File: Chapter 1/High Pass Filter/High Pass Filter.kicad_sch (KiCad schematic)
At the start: 3 parts

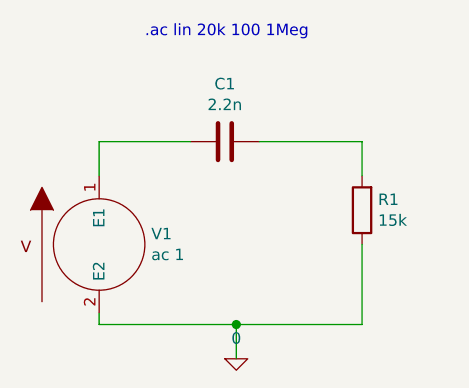
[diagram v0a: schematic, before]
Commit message: added v out tags to Chapter 1
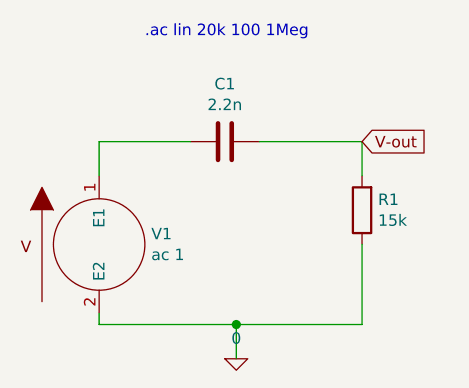
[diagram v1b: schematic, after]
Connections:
- net V-out: now reaches C1.1, R1.2
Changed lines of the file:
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@@
-(kicad_sch (version 20210406) (generator eeschema)
+(kicad_sch (version 20211123) (generator eeschema)
   (paper "A4")
-  (junction (at 95.25 63.5) (diameter 1.016) (color 0 0 0 0))
-  (wire (pts (xy 80.01 43.18) (xy 90.17 43.18))
+  (junction (at 95.25 63.5) (diameter 1.016) (color 0 0 0 0)
+  )
+  (wire (pts (xy 80.01 63.5) (xy 80.01 62.23))
+    (stroke (width 0) (type solid) (color 0 0 0 0))
+  )
+  (wire (pts (xy 109.22 63.5) (xy 95.25 63.5))
+    (stroke (width 0) (type solid) (color 0 0 0 0))
+  )
+  (wire (pts (xy 109.22 54.61) (xy 109.22 63.5))
     (stroke (width 0) (type solid) (color 0 0 0 0))
   )
@@
     (stroke (width 0) (type solid) (color 0 0 0 0))
   )
-  (wire (pts (xy 80.01 63.5) (xy 80.01 62.23))
+  (wire (pts (xy 95.25 63.5) (xy 80.01 63.5))
     (stroke (width 0) (type solid) (color 0 0 0 0))
   )
-  (wire (pts (xy 95.25 63.5) (xy 80.01 63.5))
+  (wire (pts (xy 80.01 43.18) (xy 90.17 43.18))
+    (stroke (width 0) (type solid) (color 0 0 0 0))
+  )
+  (wire (pts (xy 109.22 43.18) (xy 109.22 46.99))
+    (stroke (width 0) (type solid) (color 0 0 0 0))
+  )
+  (wire (pts (xy 97.79 43.18) (xy 109.22 43.18))
     (stroke (width 0) (type solid) (color 0 0 0 0))
   )
@@
     (stroke (width 0) (type solid) (color 0 0 0 0))
   )
-  (wire (pts (xy 97.79 43.18) (xy 109.22 43.18))
-    (stroke (width 0) (type solid) (color 0 0 0 0))
-  )
-  (wire (pts (xy 109.22 43.18) (xy 109.22 46.99))
-    (stroke (width 0) (type solid) (color 0 0 0 0))
-  )
-  (wire (pts (xy 109.22 54.61) (xy 109.22 63.5))
-    (stroke (width 0) (type solid) (color 0 0 0 0))
-  )
-  (wire (pts (xy 109.22 63.5) (xy 95.25 63.5))
-    (stroke (width 0) (type solid) (color 0 0 0 0))
-  )
   (text ".ac lin 20k 100 1Meg" (at 85.09 31.75 0)
     (effects (font (size 1.27 1.27)) (justify left bottom))
   )
-  (symbol (lib_id "High-Pass-Filter-rescue:0-pspice") (at 95.25 67.31 0) (unit 1)
+  (global_label "V-out" (shape input) (at 109.22 43.18 0) (fields_autoplaced)
+    (effects (font (size 1.27 1.27)) (justify left))
+    (property "Intersheet References" "${INTERSHEET_REFS}" (id 0) (at 117.5084 43.1006 0)
+      (effects (font (size 1.27 1.27)) (justify left) hide)
+    )
+  )
+  (symbol (lib_id "High-Pass-Filter-rescue:VSOURCE-pspice") (at 80.01 54.61 0) (unit 1)
     (in_bom yes) (on_board yes)
-    (property "Reference" "#GND01" (id 0) (at 95.25 69.85 0)
+    (property "Reference" "V1" (id 0) (at 85.8012 53.4416 0)
+      (effects (font (size 1.27 1.27)) (justify left))
+    )
+    (property "Value" "ac 1" (id 1) (at 85.8012 55.753 0)
+      (effects (font (size 1.27 1.27)) (justify left))
+    )
+    (property "Footprint" "" (id 2) (at 80.01 54.61 0)
       (effects (font (size 1.27 1.27)) hide)
     )
-    (property "Value" "0" (id 1) (at 95.25 65.0494 0))
-    (property "Footprint" "" (id 2) (at 95.25 67.31 0)
-      (effects (font (size 1.27 1.27)) hide)
-    )
-    (property "Datasheet" "~" (id 3) (at 95.25 67.31 0)
+    (property "Datasheet" "~" (id 3) (at 80.01 54.61 0)
       (effects (font (size 1.27 1.27)) hide)
     )
     (pin "1")
+    (pin "2")
+  )
+  (symbol (lib_id "High-Pass-Filter-rescue:C-Device") (at 93.98 43.18 270) (unit 1)
+    (in_bom yes) (on_board yes)
+    (property "Reference" "C1" (id 0) (at 93.98 36.7792 90))
+    (property "Value" "2.2n" (id 1) (at 93.98 39.0906 90))
+    (property "Footprint" "" (id 2) (at 90.17 44.1452 0)
+      (effects (font (size 1.27 1.27)) hide)
+    )
+    (property "Datasheet" "~" (id 3) (at 93.98 43.18 0)
+      (effects (font (size 1.27 1.27)) hide)
+    )
+    (pin "1")
+    (pin "2")
   )
   (symbol (lib_id "High-Pass-Filter-rescue:R-Device") (at 109.22 50.8 180) (unit 1)
@@
     (pin "2")
   )
-  (symbol (lib_id "High-Pass-Filter-rescue:C-Device") (at 93.98 43.18 270) (unit 1)
+  (symbol (lib_id "High-Pass-Filter-rescue:0-pspice") (at 95.25 67.31 0) (unit 1)
     (in_bom yes) (on_board yes)
-    (property "Reference" "C1" (id 0) (at 93.98 36.7792 90))
-    (property "Value" "2.2n" (id 1) (at 93.98 39.0906 90))
-    (property "Footprint" "" (id 2) (at 90.17 44.1452 0)
+    (property "Reference" "#GND01" (id 0) (at 95.25 69.85 0)
       (effects (font (size 1.27 1.27)) hide)
     )
-    (property "Datasheet" "~" (id 3) (at 93.98 43.18 0)
+    (property "Value" "0" (id 1) (at 95.25 65.0494 0))
+    (property "Footprint" "" (id 2) (at 95.25 67.31 0)
+      (effects (font (size 1.27 1.27)) hide)
+    )
+    (property "Datasheet" "~" (id 3) (at 95.25 67.31 0)
       (effects (font (size 1.27 1.27)) hide)
     )
     (pin "1")
-    (pin "2")
-  )
-  (symbol (lib_id "High-Pass-Filter-rescue:VSOURCE-pspice") (at 80.01 54.61 0) (unit 1)
-    (in_bom yes) (on_board yes)
-    (property "Reference" "V1" (id 0) (at 85.8012 53.4416 0)
-      (effects (font (size 1.27 1.27)) (justify left))
-    )
-    (property "Value" "ac 1" (id 1) (at 85.8012 55.753 0)
-      (effects (font (size 1.27 1.27)) (justify left))
-    )
-    (property "Footprint" "" (id 2) (at 80.01 54.61 0)
-      (effects (font (size 1.27 1.27)) hide)
-    )
-    (property "Datasheet" "~" (id 3) (at 80.01 54.61 0)
-      (effects (font (size 1.27 1.27)) hide)
-    )
-    (pin "1")
-    (pin "2")
   )
   (sheet_instances
